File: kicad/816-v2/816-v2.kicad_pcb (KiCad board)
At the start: 4 copper layers, 53 parts, among them J1 Barrel_Jack, J10 Mini-DIN-6, J2 UART, J3 VIA1 Port B, J4 VIA2 Connector, J5 PATA, J6 PATA_PWR, J7 Pico left, J8 Pico right, J9 DE15_Pins_HighDensity_Mountin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

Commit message: Update KiCad files
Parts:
- removed RN1, RN3: 10k, Resistor_THT:R_Array_SIP8
- added H1: MountingHole, MountingHole:MountingHole_2.2mm_M2, F.Cu at (2.54, -5.08)
- added H2: MountingHole, MountingHole:MountingHole_2.2mm_M2, F.Cu at (170.2, -5.08)
- added H3: MountingHole, MountingHole:MountingHole_2.2mm_M2, F.Cu at (170.2, 149.9)
- added H4: MountingHole, MountingHole:MountingHole_2.2mm_M2, F.Cu at (2.54, 149.9)
- added R8: 10k, Resistor_THT:R_Axial_DIN0207_L6.3mm_D2.5mm_P7.62mm_Horizontal, F.Cu at (111.8, 21.6)
- added R9: 10k, Resistor_THT:R_Axial_DIN0207_L6.3mm_D2.5mm_P7.62mm_Horizontal, F.Cu at (106.7, 21.6)
- U6: value ATtiny26L -> ATtiny26L-8P
- moved J6 159.1 mm to (5.08, 137.2), turned to 180 degrees
- moved J9 134.1 mm to (123.3, 140.9), turned to 0 degrees
- moved J5 103.4 mm to (73.7, 144.8), turned to -90 degrees
- moved R4 103.0 mm to (119.4, 120.5), turned to -90 degrees
- moved R5 103.0 mm to (114.3, 120.5), turned to -90 degrees
- moved R1 96.7 mm to (122.5, 120.5), turned to -90 degrees
- moved R3 92.8 mm to (127.6, 120.5), turned to -90 degrees
- moved J2 89.8 mm to (5.08, 119.4), turned to 180 degrees
- moved J4 77.3 mm to (55.9, 38.1)
- moved C6 74.5 mm to (7.62, 87.5)
- moved U11 74.5 mm to (27.9, 121.9)
- moved C8 65.6 mm to (99.1, 90.2)
- moved U8 65.6 mm to (48.3, 90.2)
- moved C7 65.6 mm to (68.7, 90.2)
- moved U13 65.6 mm to (78.7, 90.2)
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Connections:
- U1 pad 3: Net-(RN1-R6) -> VCC
- U1 pad 36: Net-(RN1-R4) -> VCC
- U1 pad 6: Net-(RN1-R5) -> VCC
- U10 pad 24: Net-(RN3-R3) -> VCC
- U11 pad 2: Net-(RN3-R1) -> VCC
- U11 pad 26: IRQ3 -> unconnected-(U11-~{IRQ}-Pad26)
- U2 pad 1: Net-(RN1-R3) -> VCC
- U2 pad 4: Net-(RN1-R3) -> VCC
- U5 pad 1: A23 -> PH2
- U5 pad 11: A16 -> A14
- U5 pad 12: VDA -> A13
- U5 pad 14: A15 -> A12
- U5 pad 16: A14 -> A11
- U5 pad 17: A13 -> A10
- U5 pad 18: A12 -> A8
- U5 pad 19: A11 -> A9
- U5 pad 2: A22 -> VDA
- U5 pad 20: A10 -> A6
- U5 pad 21: A9 -> A7
- U5 pad 24: A8 -> A4
- U5 pad 25: A7 -> A5
- U5 pad 26: A6 -> OE
- U5 pad 27: A5 -> WE
- U5 pad 28: A4 -> ROMCS
- U5 pad 29: ROMCS -> RAMCS
- U5 pad 31: RAMCS -> IO4CS
- U5 pad 33: IO1CS -> A16
- U5 pad 34: IO2CS -> A17
- U5 pad 36: IO3CS -> A18
- U5 pad 37: IO4CS -> A19
- U5 pad 39: IO5CS -> A20
- U5 pad 4: A21 -> IO1CS
- U5 pad 40: OE -> A22
- U5 pad 41: WE -> A21
- U5 pad 43: PH2 -> A23
- U5 pad 5: A20 -> A15
- U5 pad 6: A19 -> IO2CS
- U5 pad 8: A18 -> IO3CS
- U5 pad 9: A17 -> IO5CS
- U9 pad 24: Net-(RN3-R2) -> VCC
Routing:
- net RESB: track 0.00 -> 371.7 mm, vias 0 -> 4
- net D3: track 0.00 -> 338.8 mm, vias 0 -> 1
- net RWB: track 0.00 -> 335.9 mm, vias 0 -> 4
- net A1: track 0.00 -> 335.1 mm, vias 0 -> 1
- net D4: track 0.00 -> 333.3 mm, vias 0 -> 1
- net D2: track 0.00 -> 327.9 mm
- net D7: track 0.00 -> 323.4 mm, vias 0 -> 1
- net D5: track 0.00 -> 317.4 mm, vias 0 -> 1
- net A0: track 0.00 -> 317.2 mm, vias 0 -> 1
- net D6: track 0.00 -> 313.7 mm, vias 0 -> 1
- net D1: track 0.00 -> 313.1 mm
- net D0: track 0.00 -> 302.8 mm
- net PH2: track 0.00 -> 279.4 mm, vias 0 -> 4
- net A2: track 0.00 -> 261.4 mm
- net A3: track 0.00 -> 165.9 mm
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- added copper zone on In1.Cu, net GND
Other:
- board outline added: 172.7 x 160 mm
- board text added: "WayWayWay"

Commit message: Update KiCad files
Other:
- board text added: "'245"
- board text added: "'573"
- board text added: "'74"
- board text added: "ACIA"
- board text added: "ATtiny26L"
- board text added: "GND +5V"
- board text added: "GND RX TX +5V"
- board text added: "RAM"
- board text added: "ROM"
- board text added: "VIA 1"
- board text added: "VIA 2"
- board text added: "VIA1 Port B --------- +5V | PB0 PB1 | PB2 PB3 | PB4 PB5 | PB6 PB7 | GND CB1 | CB2"
- board text added: "VIA2 --------- +5V | PA0 PA1 | PA2 PA3 | PA4 PA5 | PA6 PA7 | GND CA1 | CA2 PB0 | PB1 PB2 | PB3 PB4 | PB5 PB6 | PB7 GND | CB1 CB2 | GND"
- board text added: "W65C816S"
- board text removed: "WayWayWay"
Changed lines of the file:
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@@
 		(layer "Edge.Cuts")
 	)
-	(gr_text "WayWayWay"
-		(at 132.08 5.08 0)
+	(gr_text "VIA1 Port B\n---------\n+5V | PB0\nPB1 | PB2\nPB3 | PB4\nPB5 | PB6\nPB7 | GND\nCB1 | CB2"
+		(at 157.48 58.42 0)
+		(layer "F.SilkS")
+		(effects
+			(font
+				(size 1 1)
+				(thickness 0.1)
+			)
+			(justify bottom)
+		)
+	)
+	(gr_text "GND\nRX\nTX\n+5V"
+		(at 7.62 119.38 0)
 		(layer "F.SilkS")
 		(effects
@@
 		)
 	)
+	(gr_text "VIA 2"
+		(at 73.66 35.56 0)
+		(layer "F.SilkS")
+		(effects
+			(font
+				(size 1 1)
+				(thickness 0.1)
+			)
+			(justify left bottom)
+		)
+	)
+	(gr_text "ATtiny26L"
+		(at 21.59 48.26 90)
+		(layer "F.SilkS")
+		(effects
+			(font
+				(size 1 1)
+				(thickness 0.1)
+			)
+			(justify left bottom)
+		)
+	)
+	(gr_text "VIA 1"
+		(at 40.64 35.56 0)
+		(layer "F.SilkS")
+		(effects
+			(font
+				(size 1 1)
+				(thickness 0.1)
+			)
+			(justify left bottom)
+		)
+	)
+	(gr_text "GND\n+5V"
+		(at 10.16 138.54 0)
+		(layer "F.SilkS")
+		(effects
+			(font
+				(size 1 1)
+				(thickness 0.1)
+			)
+			(justify left bottom)
+		)
+	)
+	(gr_text "ACIA"
+		(at 17.78 119.38 0)
+		(layer "F.SilkS")
+		(effects
+			(font
+				(size 1 1)
+				(thickness 0.1)
+			)
+			(justify left bottom)
+		)
+	)
+	(gr_text "'573"
+		(at 142.24 59.69 270)
+		(layer "F.SilkS")
+		(effects
+			(font
+				(size 1 1)
+				(thickness 0.1)
+			)
+			(justify left bottom)
+		)
+	)
+	(gr_text "'245"
+		(at 104.14 60.96 270)
+		(layer "F.SilkS")
+		(effects
+			(font
+				(size 1 1)
+				(thickness 0.1)
+			)
+			(justify left bottom)
+		)
+	)
+	(gr_text "W65C816S"
+		(at 116.84 38.1 0)
+		(layer "F.SilkS")
+		(effects
+			(font
+				(size 1 1)
+				(thickness 0.1)
+			)
+			(justify left bottom)
+		)
+	)
+	(gr_text "'74"
+		(at 142.24 33.02 270)
+		(layer "F.SilkS")
+		(effects
+			(font
+				(size 1 1)
+				(thickness 0.1)
+			)
+			(justify left bottom)
+		)
+	)
+	(gr_text "RAM"
+		(at 83.82 96.52 0)
+		(layer "F.SilkS")
+		(effects
+			(font
+				(size 1 1)
+				(thickness 0.1)
+			)
+			(justify left bottom)
+		)
+	)
+	(gr_text "ROM"
+		(at 53.34 96.52 0)
+		(layer "F.SilkS")
+		(effects
+			(font
+				(size 1 1)
+				(thickness 0.1)
+			)
+			(justify left bottom)
+		)
+	)
+	(gr_text "VIA2\n---------\n+5V | PA0\nPA1 | PA2\nPA3 | PA4\nPA5 | PA6\nPA7 | GND\nCA1 | CA2\nPB0 | PB1\nPB2 | PB3\nPB4 | PB5\nPB6 | PB7\nGND | CB1\nCB2 | GND"
+		(at 157.48 43.18 0)
+		(layer "F.SilkS")
+		(effects
+			(font
+				(size 1 1)
+				(thickness 0.1)
+			)
+			(justify bottom)
+		)
+	)

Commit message: Update KiCad files new pcb revision, hopefully working
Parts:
- added C10: 0.1uF, Capacitor_THT:C_Disc_D4.3mm_W1.9mm_P5.00mm, F.Cu at (92.0, 56.5)
- H1, H2, H3, H4: footprint MountingHole:MountingHole_2.2mm_M2 -> MountingHole:MountingHole_3.2mm_M3
- J9: value DE15_Pins_HighDensity_MountingHoles -> DE-15 HD
- U1: value W65C816SxP -> W65C816
- U10, U9: value W65C22NxP -> W65C22S
- U11: value W65C51NxP -> W65C51
- U13: value AS6C4008-55PCN -> AS6C4008
- U5: value ATF1504AS-10JU44 -> ATF1504AS
- U6: value ATtiny26L-8P -> ATtiny26L
- VR1: value UA78L05ACPK -> 7805
- Y2: footprint Package_DIP:DIP-8_W7.62mm_Socket -> Oscillator:Oscillator_DIP-8
- moved D2 145.9 mm to (163.1, 33.6), turned to -90 degrees
- moved R2 126.4 mm to (158.0, 29.8), turned to -90 degrees
- moved C4 107.3 mm to (150.4, 31.0), turned to -90 degrees
- moved D1 103.6 mm to (135.1, 37.8)
- moved C2 103.4 mm to (135.2, 31.0)
- moved C3 103.3 mm to (145.3, 31.0)
- moved U12 92.2 mm to (173.3, 26.0), turned to 0 degrees
- moved C7 90.2 mm to (158.0, 102.2), turned to -90 degrees
- moved C6 90.0 mm to (97.2, 97.1), turned to 0 degrees
- moved VR1 85.9 mm to (125.0, 31.0), turned to 0 degrees
- moved SW2 85.1 mm to (172.6, 31.3)
- moved J3 82.5 mm to (102.2, 74.2)
- moved J6 82.0 mm to (84.4, 158.0), turned to 90 degrees
- moved R6 80.9 mm to (85.7, 66.6)
- moved R7 80.9 mm to (85.7, 71.7)
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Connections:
- C14 pad 1: VCC -> GND
- C14 pad 2: GND -> VCC
- C9 pad 1: VCC -> GND
- C9 pad 2: GND -> VCC
- J10 pad 1: Net-(J10-Pad1) -> PS2DATA
- J10 pad 5: Net-(J10-Pad5) -> PS2CLK
- J7 pad 19: A0 -> unconnected-(J7-Pin_19-Pad19)
- J7 pad 20: A1 -> unconnected-(J7-Pin_20-Pad20)
- R6 pad 1: Net-(J10-Pad5) -> VCC
- R7 pad 1: Net-(J10-Pad1) -> VCC
- U5 pad 1: PH2 -> A15
- U5 pad 11: A14 -> A13
- U5 pad 12: A13 -> A12
- U5 pad 14: A12 -> A11
- U5 pad 16: A11 -> A10
- U5 pad 17: A10 -> A9
- U5 pad 18: A8 -> A7
- U5 pad 19: A9 -> A8
- U5 pad 20: A6 -> A5
- U5 pad 21: A7 -> A6
- U5 pad 24: A4 -> IO5CS
- U5 pad 25: A5 -> A4
- U5 pad 27: WE -> A23
- U5 pad 28: ROMCS -> RAMCS
- U5 pad 29: RAMCS -> ROMCS
- U5 pad 33: A16 -> WE
- U5 pad 34: A17 -> A22
- U5 pad 36: A18 -> A20
- U5 pad 37: A19 -> A21
- U5 pad 39: A20 -> A19
- U5 pad 4: IO1CS -> IO2CS
- U5 pad 40: A22 -> A17
- U5 pad 41: A21 -> A18
- U5 pad 43: A23 -> A16
- U5 pad 5: A15 -> PH2
- U5 pad 6: IO2CS -> IO1CS
- U5 pad 9: IO5CS -> A14
- U8 pad 28: A13 -> GND
- U8 pad 29: A14 -> GND
- U8 pad 3: A15 -> GND
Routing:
- net VCC: track 778.8 -> 0.00 mm
- net D7: track 323.4 -> 208.0 mm
- net D4: track 333.3 -> 230.6 mm
- net D6: track 313.7 -> 216.5 mm
- net D3: track 338.8 -> 242.7 mm, vias 1 -> 0
- net D5: track 317.4 -> 224.4 mm
- net D2: track 327.9 -> 254.2 mm, vias 0 -> 1
- net BLUE: track 29.0 -> 102.0 mm
- net PH2: track 279.4 -> 350.9 mm, vias 4 -> 1
- net IO5CS: track 133.9 -> 64.6 mm, vias 4 -> 0
- net GREEN2: track 33.2 -> 99.2 mm
- net RED: track 22.9 -> 88.8 mm
- net A1: track 335.1 -> 269.3 mm
- net GREEN1: track 39.4 -> 90.0 mm
- net A2: track 261.4 -> 212.1 mm, vias 0 -> 1
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- added copper zone on In2.Cu, net GND
- added copper zone on B.Cu, net VCC
- added copper zone on F.Cu, net VCC
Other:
- board size 172.7 x 160 mm -> 154.9 x 142.2 mm
- board text added: "+5V GND"
- board text added: "+5v TX RX GND"
- board text added: "245"
- board text added: "573"
- board text added: "74"
- board text added: "816 rev 2 12-feb-2026"
- board text added: "ATF1504AS"
- board text added: "CPU"
- board text added: "PATA"
- board text added: "PATA Power"
- board text added: "Pico 2 Front -->"
- board text added: "VIA 1 Port B -------- +5v | PB0 PB1 | PB2 PB3 | PB4 PB5 | PB6 PB7 | GND CB1 | CB2"
- board text added: "VIA 2 Port A & B ----------- +5V | PA0 PA1 | PA2 PA3 | PA4 PA5 | PA6 PA7 | GND CA1 | CA2 PB0 | PB1 PB2 | PB3 PB4 | PB5 PB6 | PB7 GND | CB1 CB2 | GND"
- board text removed: "'245"
- board text removed: "'573"
- board text removed: "'74"
- board text removed: "ATtiny26L"
- board text removed: "GND +5V"
- board text removed: "GND RX TX +5V"
- board text removed: "VIA1 Port B --------- +5V | PB0 PB1 | PB2 PB3 | PB4 PB5 | PB6 PB7 | GND CB1 | CB2"
- board text removed: "VIA2 --------- +5V | PA0 PA1 | PA2 PA3 | PA4 PA5 | PA6 PA7 | GND CA1 | CA2 PB0 | PB1 PB2 | PB3 PB4 | PB5 PB6 | PB7 GND | CB1 CB2 | GND"
- board text removed: "W65C816S"

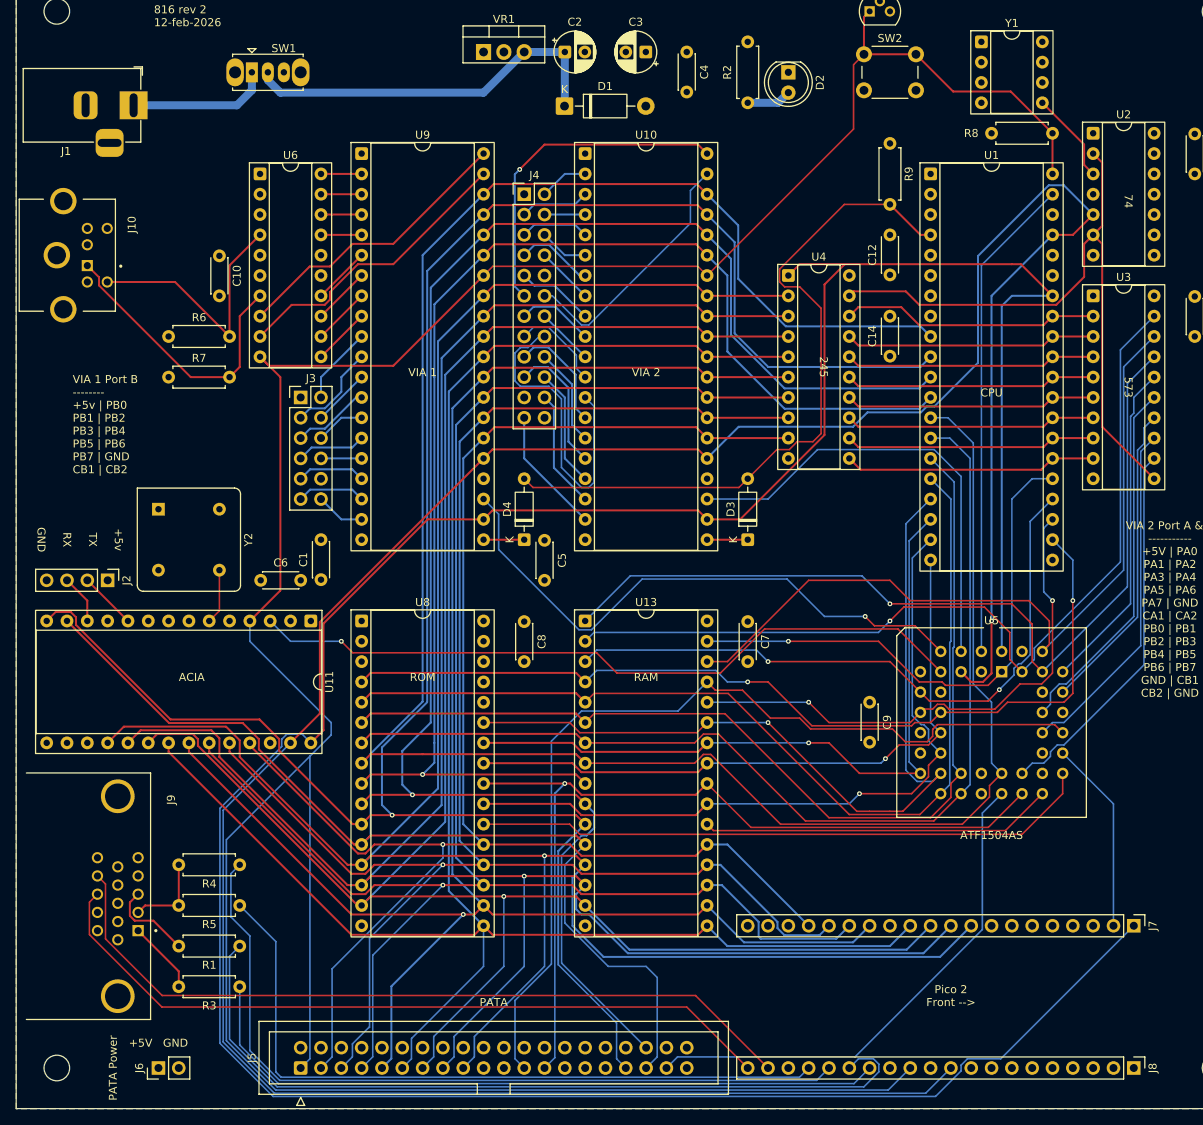
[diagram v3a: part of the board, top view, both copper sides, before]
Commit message: Update KiCad files to reflect ROM WE bodge
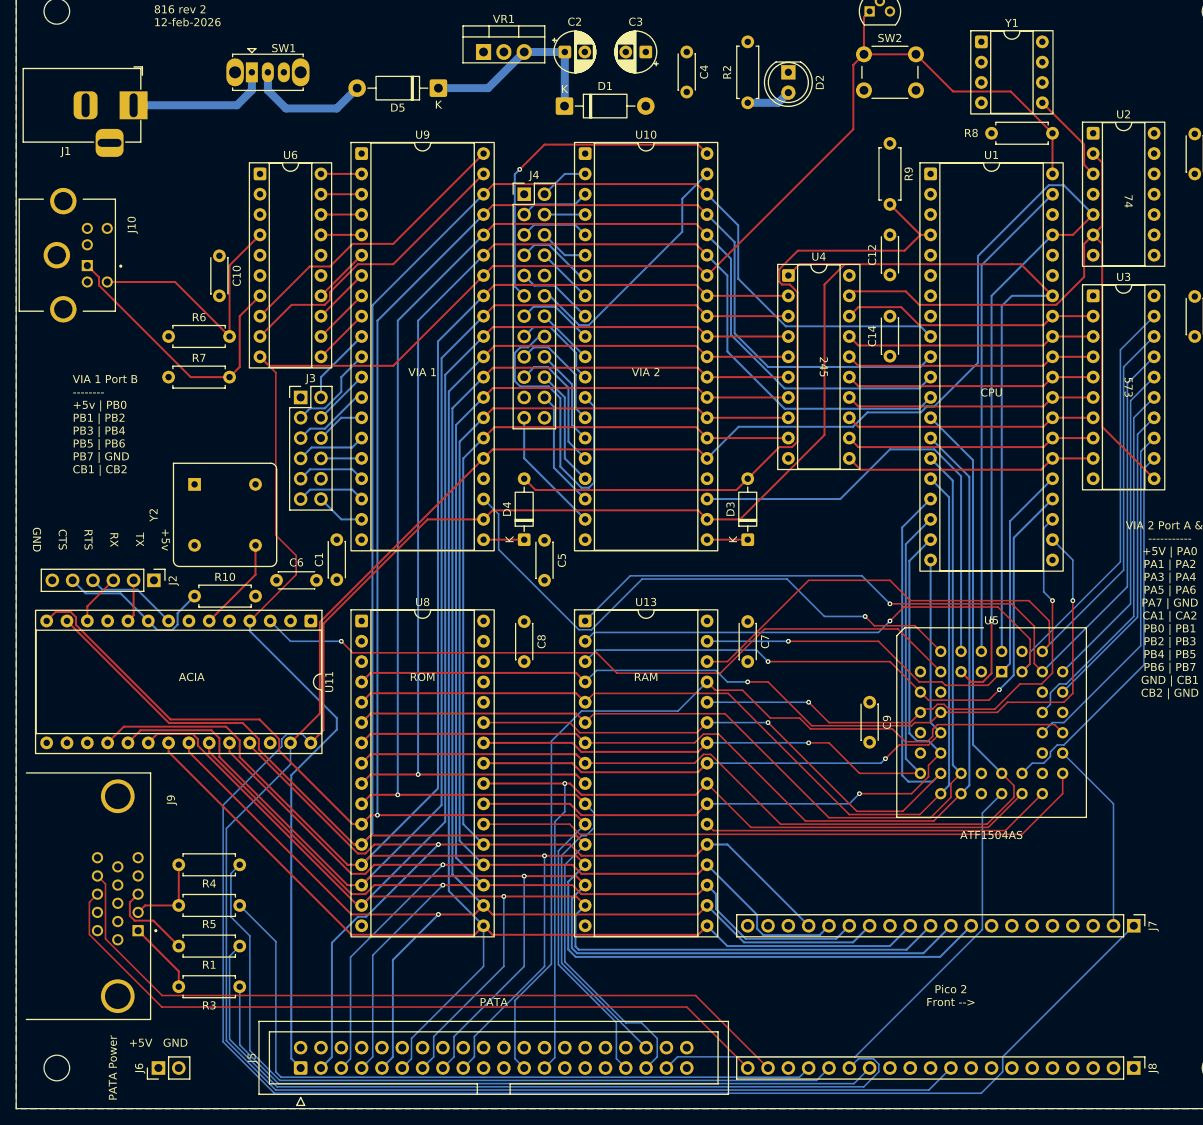
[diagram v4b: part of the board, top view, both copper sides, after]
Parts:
- added D5: 1N4001, Diode_THT:D_DO-41_SOD81_P10.16mm_Horizontal, F.Cu at (119.4, 35.6)
- added R10: 10K, Resistor_THT:R_Axial_DIN0207_L6.3mm_D2.5mm_P7.62mm_Horizontal, F.Cu at (88.9, 99.1)
- J2: footprint Connector_PinHeader_2.54mm:PinHeader_1x04_P2.54mm_Vertical -> Connector_PinHeader_2.54mm:PinHeader_1x06_P2.54mm_Vertical
- moved J2 5.79 mm to (83.8, 97.1)
- moved Y2 5.48 mm to (88.9, 85.1)
- moved C1 1.98 mm to (106.7, 97.0)
- moved C6 1.98 mm to (99.1, 97.1)
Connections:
- net IO1CS renamed ~{IO1CS}
- net IO2CS renamed ~{IO2CS}
- net IO3CS renamed ~{IO3CS}
- net IO4CS renamed ~{IO4CS}
- net IO5CS renamed ~{IO5CS}
- net IRQB renamed ~{IRQ}
- net OE renamed ~{OE}
- net PH2B renamed ~{PH2}
- net PS2CLK renamed Net-(U6-PB3)
- net PS2DATA renamed Net-(U6-XTAL1/PB4)
- net RAMCS renamed ~{RAMCS}
- net ROMCS renamed ~{ROMCS}
- net RWB renamed R/~{W}
- net WE renamed ~{WE}
- J2 pad 4: GND -> Net-(J2-Pin_4)
- J5 pad 1: RESB -> ~{RES}
- J7 pad 18: GND -> unconnected-(J7-Pin_18-Pad18)
- J7 pad 3: GND -> unconnected-(J7-Pin_3-Pad3)
- J7 pad 8: GND -> unconnected-(J7-Pin_8-Pad8)
- J8 pad 12: RESB -> unconnected-(J8-Pin_12-Pad12)
- J8 pad 13: GND -> unconnected-(J8-Pin_13-Pad13)
- J8 pad 18: GND -> unconnected-(J8-Pin_18-Pad18)
- J8 pad 3: GND -> unconnected-(J8-Pin_3-Pad3)
- J8 pad 8: GND -> unconnected-(J8-Pin_8-Pad8)
- R8 pad 2: RESB -> ~{RES}
- SW1 pad 2: Net-(D1-K) -> Net-(D5-A)
- SW2 pad 1: RESB -> ~{RES}
- U1 pad 40: RESB -> ~{RES}
- U10 pad 34: RESB -> ~{RES}
- U11 pad 4: RESB -> ~{RES}
- U11 pad 8: unconnected-(U11-~{RTS}-Pad8) -> Net-(J2-Pin_4)
- U11 pad 9: GND -> Net-(J2-Pin_5)
- U12 pad 1: RESB -> ~{RES}
- U6 pad 10: RESB -> ~{RES}
- U8 pad 31: unconnected-(U8-PGM-Pad31) -> VCC
- U9 pad 34: RESB -> ~{RES}
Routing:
- net RESB: track 362.5 -> 0.00 mm
- net ~{RES}: track 0.00 -> 236.7 mm
- net Net-(D1-K): track 47.7 -> 24.5 mm
- net Net-(J2-Pin_5): track 0.00 -> 20.4 mm
- net Net-(D5-A): track 0.00 -> 15.4 mm
- net Net-(J2-Pin_4): track 0.00 -> 11.6 mm
- net Net-(U11-XTAL1): track 6.88 -> 11.9 mm
- net D2: track 254.2 -> 259.0 mm
- net D1: track 267.0 -> 270.6 mm
- net D0: track 278.6 -> 281.1 mm
- net A16: track 113.0 -> 114.8 mm
- net Net-(J2-Pin_2): track 7.18 -> 5.37 mm
- net A4: track 137.9 -> 139.7 mm
- net A0: track 270.9 -> 269.3 mm
- net ~{IRQ}: track 88.0 -> 86.4 mm
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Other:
- board text added: "+5v TX RX RTS CTS GND"
- board text removed: "+5v TX RX GND"
